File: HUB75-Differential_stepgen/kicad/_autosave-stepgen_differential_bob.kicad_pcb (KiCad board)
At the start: 2 copper layers, 85 x 56 mm, 35 parts, among them J1 Conn_02x08_Odd_Even, J2 Conn_02x08_Odd_Even, J3 Conn_02x08_Odd_Even, J4 Screw_Terminal_01x02, J5 RJ45_LED, J6 RJ45_LED, J7 RJ45_LED, SW1 SW_DIP_x03, SW2 SW_DIP_x03, U1 74HC86, U2 74HC86

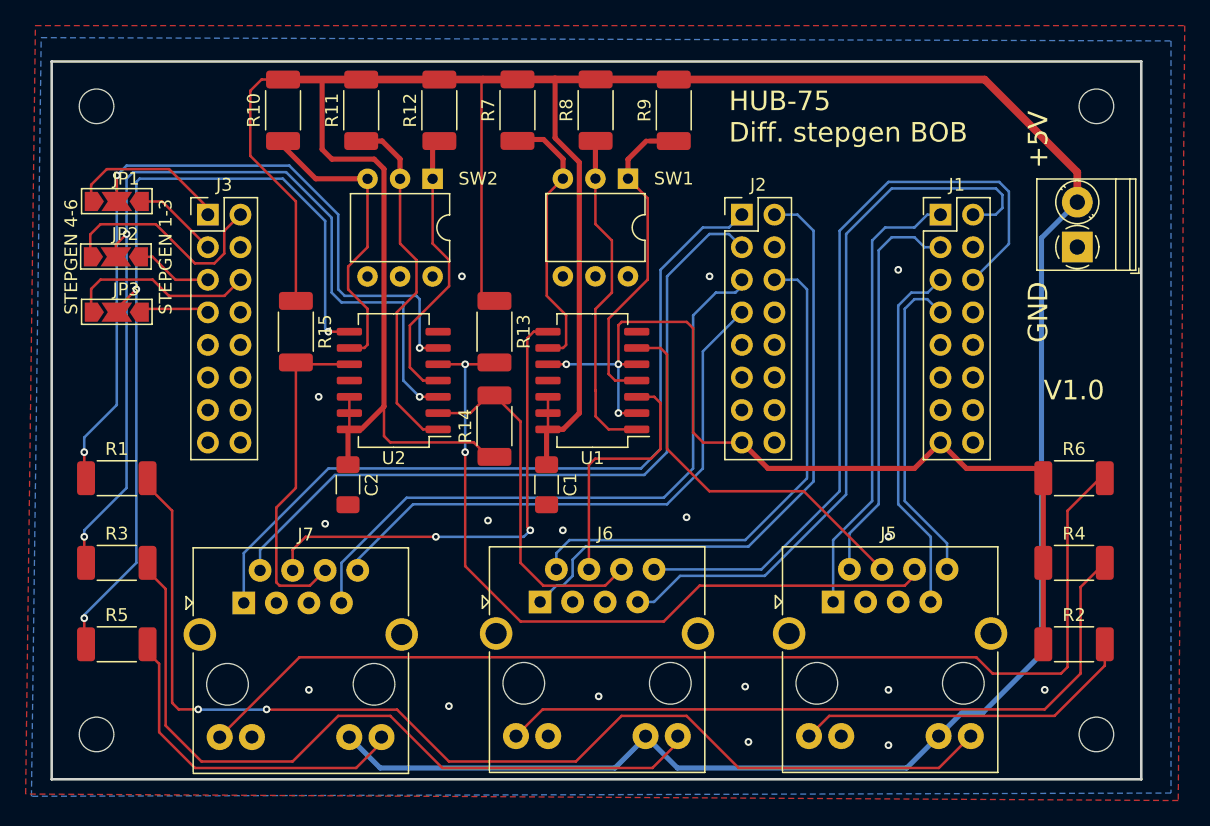
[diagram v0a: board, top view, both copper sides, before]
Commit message: Smaller resistors + production ready
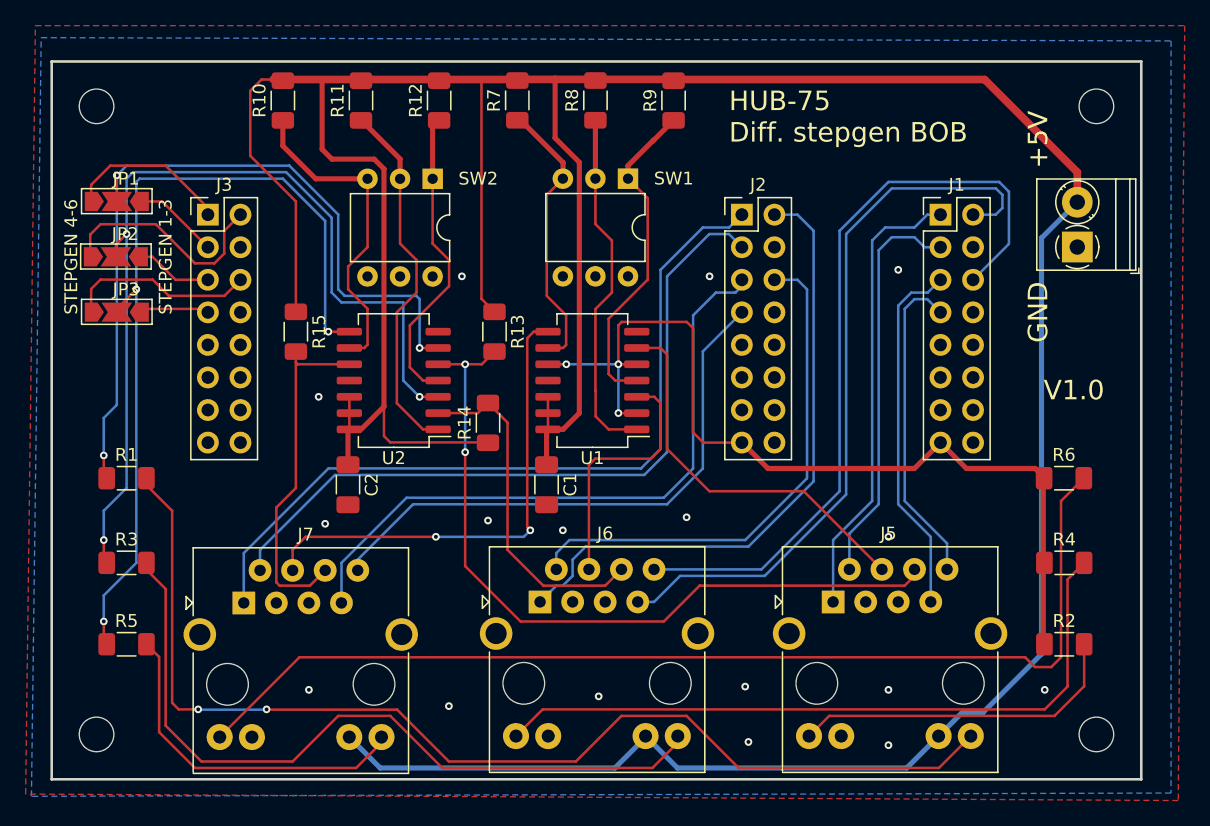
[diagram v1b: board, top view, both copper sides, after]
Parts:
- R1, R10, R11, R12, R13, R14, R15, R2, R3, R4, R5, R6, R7, R8, R9: footprint Resistor_SMD:R_2010_5025Metric_Pad1.40x2.65mm_HandSolder -> Resistor_SMD:R_1206_3216Metric_Pad1.30x1.75mm_HandSolder
- moved R6 0.79 mm to (79.0, 32.5)
- moved R10 0.76 mm to (18.0, 3.05)
- moved R11 0.76 mm to (24.1, 3.05)
- moved R12 0.76 mm to (30.2, 3.05)
- moved R7 0.76 mm to (36.3, 3.04)
- moved R8 0.76 mm to (42.4, 3.04)
- moved R9 0.76 mm to (48.5, 3.05)
- moved R2 0.76 mm to (79.0, 45.5)
- moved R4 0.76 mm to (79.0, 39.1)
- moved R1 0.76 mm to (5.84, 32.5)
- moved R3 0.76 mm to (5.84, 39.1)
- moved R5 0.76 mm to (5.84, 45.5)
- moved R14 0.57 mm to (34.0, 28.2)
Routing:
- net Net-(J7-Pad12): track 85.6 -> 83.5 mm
- net +5V: track 286.6 -> 288.5 mm
- net Net-(R8-Pad1): track 26.2 -> 27.8 mm
- net Net-(R10-Pad1): track 23.8 -> 25.4 mm
- net Net-(R12-Pad1): track 22.3 -> 23.9 mm
- net Net-(J7-Pad9): track 25.4 -> 26.6 mm
- net ALARM3: track 26.4 -> 27.3 mm
- net ALARM1: track 58.0 -> 58.9 mm
- net Net-(R9-Pad1): track 25.0 -> 25.7 mm
- net Net-(R11-Pad1): track 27.9 -> 28.6 mm
- net Net-(J6-Pad12): track 55.5 -> 54.8 mm
- net Net-(J5-Pad12): track 27.0 -> 26.3 mm
- net ALARM2: track 27.5 -> 26.9 mm
- net ALARM_OK3: track 66.1 -> 65.5 mm
- net ALARM_OK1: track 63.0 -> 62.4 mm
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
